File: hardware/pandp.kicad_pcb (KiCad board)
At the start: 2 copper layers, 116 x 55.5 mm, 94 parts, among them IC1 ADP2303-5, IC2 DRV8830, P1 CONN_01X02, P10 CONN_01X04, P11 CONN_01X02, P12 CONN_02X04, P13 CONN_01X02, P14 CONN_01X04, P15 CONN_01X04, P16 CONN_01X03, P17 CONN_01X03, P18 CONN_01X03, P19 CONN_01X03, P2 CONN_01X03, P20 CONN_01X03, P21 CONN_01X03, P22 CONN_02X03, P23 CONN_02X03, P24 CONN_02X03, P25 CONN_02X03, P26 CONN_01X03, P27 CONN_01X03, P28 CONN_01X03, P29 CONN_01X03, P3 CONN_01X02, P30 CONN_01X04, P31 CONN_01X04, P32 CONN_01X04, P33 CONN_01X04, P4 CONN_01X03, P5 CONN_01X02, P6 CONN_01X03, P7 CONN_01X03, P8 USB_OTG, P9 CONN_01X02, Q1 IRF540N, Q2 IRF540N, SW1 SW_PUSH, U1 AP1117D33, U2 STM32F103RC, Y1 Crystal_Small - 2101357 on el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, Y2 Crystal_Small - 2063972 on el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

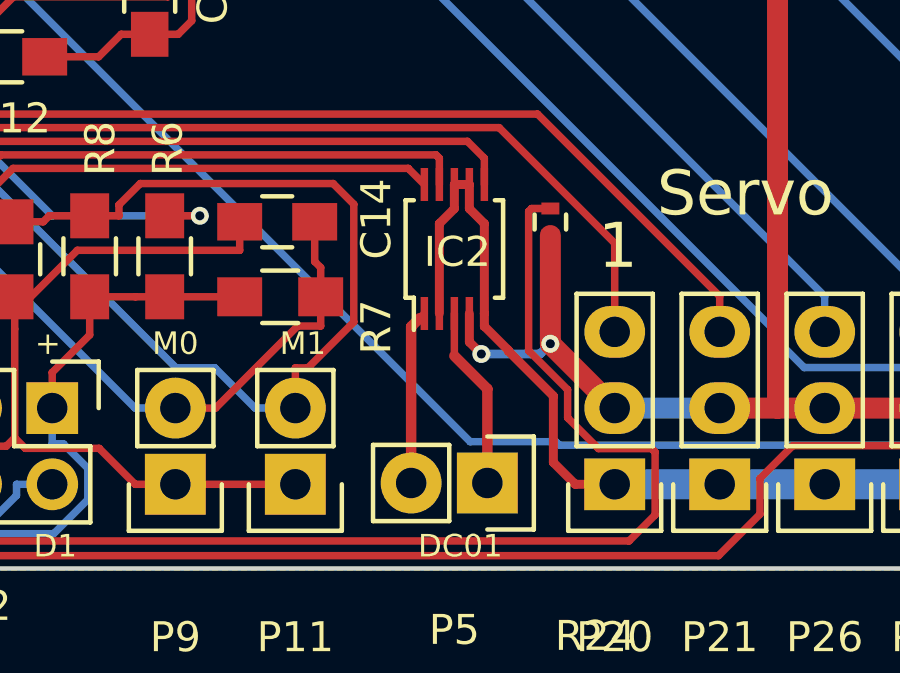
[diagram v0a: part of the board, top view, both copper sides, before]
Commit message: changed a few small routes, added vias for cooling on dc conroller
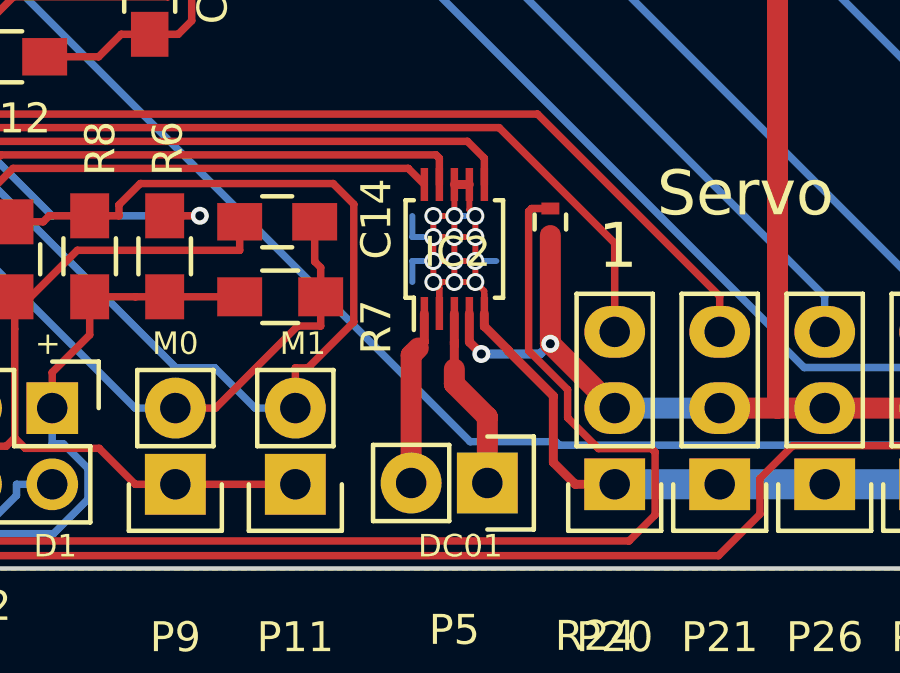
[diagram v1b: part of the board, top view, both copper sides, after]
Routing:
- net GND: track 435.9 -> 449.7 mm, vias 0 -> 12
